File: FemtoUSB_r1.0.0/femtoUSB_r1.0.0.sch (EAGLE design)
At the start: 24 parts, among them IC1 ATSAMD21E18A-MUT

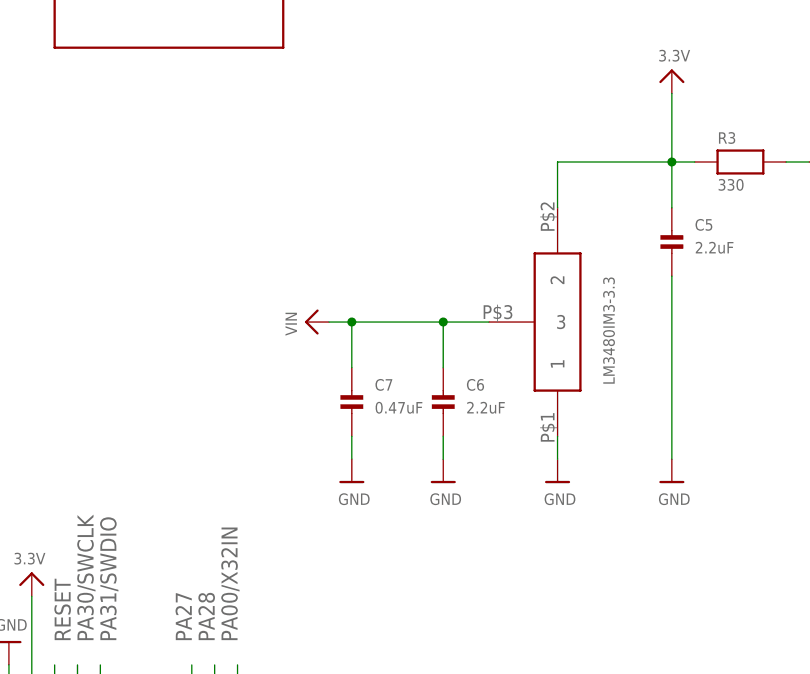
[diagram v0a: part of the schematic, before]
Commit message: Corrected the Make and model of the LDO Voltage Regulator. Board now powers on.
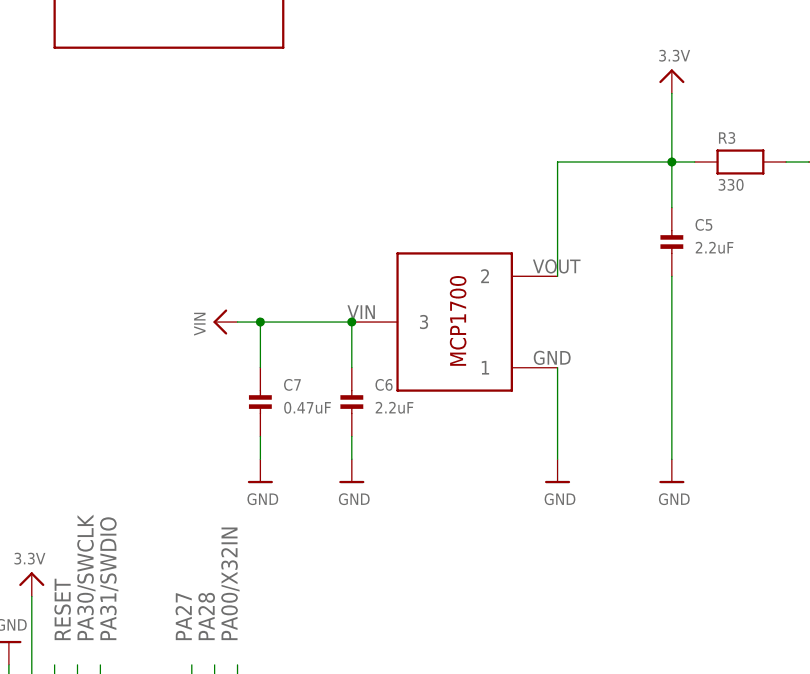
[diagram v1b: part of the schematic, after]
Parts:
- LDO_VREG: value LM3480 -> MCP1700T-3302E/TT; device ti-lm3480:LM3480 -> MCP1700T-3302E_TT:MCP1700T-3302E/TT
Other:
- moved on the sheet: C6, C7
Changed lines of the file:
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@@
 <part name="U$26" library="microbuilder" deviceset="GND" device=""/>
 <part name="U$27" library="microbuilder" deviceset="GND" device=""/>
-<part name="LDO_VREG" library="ti-lm3480" deviceset="LM3480" device=""/>
+<part name="LDO_VREG" library="MCP1700T-3302E_TT" deviceset="MCP1700T-3302E/TT" device=""/>
 <part name="U$3" library="microbuilder" deviceset="GND" device=""/>
 <part name="C5" library="microbuilder" deviceset="CAP_CERAMIC" device="_0402MP" value="2.2uF"/>
@@
 <instance part="U$26" gate="G$1" x="180.34" y="121.92" rot="R180"/>
 <instance part="U$27" gate="G$1" x="226.06" y="99.06"/>
-<instance part="LDO_VREG" gate="G$1" x="106.68" y="96.52" rot="R270"/>
+<instance part="LDO_VREG" gate="G$1" x="104.14" y="96.52" rot="R180"/>
 <instance part="U$3" gate="G$1" x="149.86" y="106.68" rot="R90"/>
 <instance part="C5" gate="G$1" x="121.92" y="96.52"/>
 <instance part="U$4" gate="G$1" x="121.92" y="116.84"/>
 <instance part="U$28" gate="G$1" x="109.22" y="71.12"/>
-<instance part="U$29" gate="G$1" x="81.28" y="88.9" rot="R90"/>
+<instance part="U$29" gate="G$1" x="71.12" y="88.9" rot="R90"/>
 <instance part="U$30" gate="G$1" x="121.92" y="71.12"/>
-<instance part="C6" gate="G$1" x="96.52" y="78.74"/>
-<instance part="C7" gate="G$1" x="86.36" y="78.74"/>
-<instance part="U$31" gate="G$1" x="96.52" y="71.12"/>
-<instance part="U$32" gate="G$1" x="86.36" y="71.12"/>
+<instance part="C6" gate="G$1" x="86.36" y="78.74"/>
+<instance part="C7" gate="G$1" x="76.2" y="78.74"/>
+<instance part="U$31" gate="G$1" x="86.36" y="71.12"/>
+<instance part="U$32" gate="G$1" x="76.2" y="71.12"/>
 <instance part="U$33" gate="G$1" x="198.12" y="43.18"/>
 <instance part="U$34" gate="G$1" x="172.72" y="165.1" rot="R90"/>
@@
 <pinref part="LDO_VREG" gate="G$1" pin="1"/>
 <pinref part="U$28" gate="G$1" pin="GND"/>
-<wire x1="109.22" y1="73.66" x2="109.22" y2="76.2" width="0.1524" layer="91"/>
+<wire x1="109.22" y1="73.66" x2="109.22" y2="83.82" width="0.1524" layer="91"/>
 </segment>
 <segment>
@@
 <pinref part="C6" gate="G$1" pin="P$2"/>
 <pinref part="U$31" gate="G$1" pin="GND"/>
-<wire x1="96.52" y1="76.2" x2="96.52" y2="73.66" width="0.1524" layer="91"/>
+<wire x1="86.36" y1="76.2" x2="86.36" y2="73.66" width="0.1524" layer="91"/>
 </segment>
 <segment>
 <pinref part="C7" gate="G$1" pin="P$2"/>
 <pinref part="U$32" gate="G$1" pin="GND"/>
-<wire x1="86.36" y1="76.2" x2="86.36" y2="73.66" width="0.1524" layer="91"/>
+<wire x1="76.2" y1="76.2" x2="76.2" y2="73.66" width="0.1524" layer="91"/>
 </segment>
 <segment>
@@
 <pinref part="U$4" gate="G$1" pin="3.3V"/>
 <pinref part="LDO_VREG" gate="G$1" pin="2"/>
-<wire x1="109.22" y1="101.6" x2="109.22" y2="106.68" width="0.1524" layer="91"/>
+<wire x1="109.22" y1="93.98" x2="109.22" y2="106.68" width="0.1524" layer="91"/>
 <wire x1="109.22" y1="106.68" x2="121.92" y2="106.68" width="0.1524" layer="91"/>
 </segment>
@@
 <segment>
 <pinref part="LDO_VREG" gate="G$1" pin="3"/>
-<wire x1="101.6" y1="88.9" x2="96.52" y2="88.9" width="0.1524" layer="91"/>
-<junction x="96.52" y="88.9"/>
-<wire x1="96.52" y1="88.9" x2="86.36" y2="88.9" width="0.1524" layer="91"/>
 <junction x="86.36" y="88.9"/>
-<wire x1="86.36" y1="88.9" x2="83.82" y2="88.9" width="0.1524" layer="91"/>
+<wire x1="86.36" y1="88.9" x2="76.2" y2="88.9" width="0.1524" layer="91"/>
+<junction x="76.2" y="88.9"/>
+<wire x1="76.2" y1="88.9" x2="73.66" y2="88.9" width="0.1524" layer="91"/>
 <pinref part="U$29" gate="G$1" pin="VIN"/>
+<wire x1="76.2" y1="88.9" x2="76.2" y2="83.82" width="0.1524" layer="91"/>
 <wire x1="86.36" y1="88.9" x2="86.36" y2="83.82" width="0.1524" layer="91"/>
-<wire x1="96.52" y1="88.9" x2="96.52" y2="83.82" width="0.1524" layer="91"/>
 <pinref part="C6" gate="G$1" pin="P$1"/>
 <pinref part="C7" gate="G$1" pin="P$1"/>

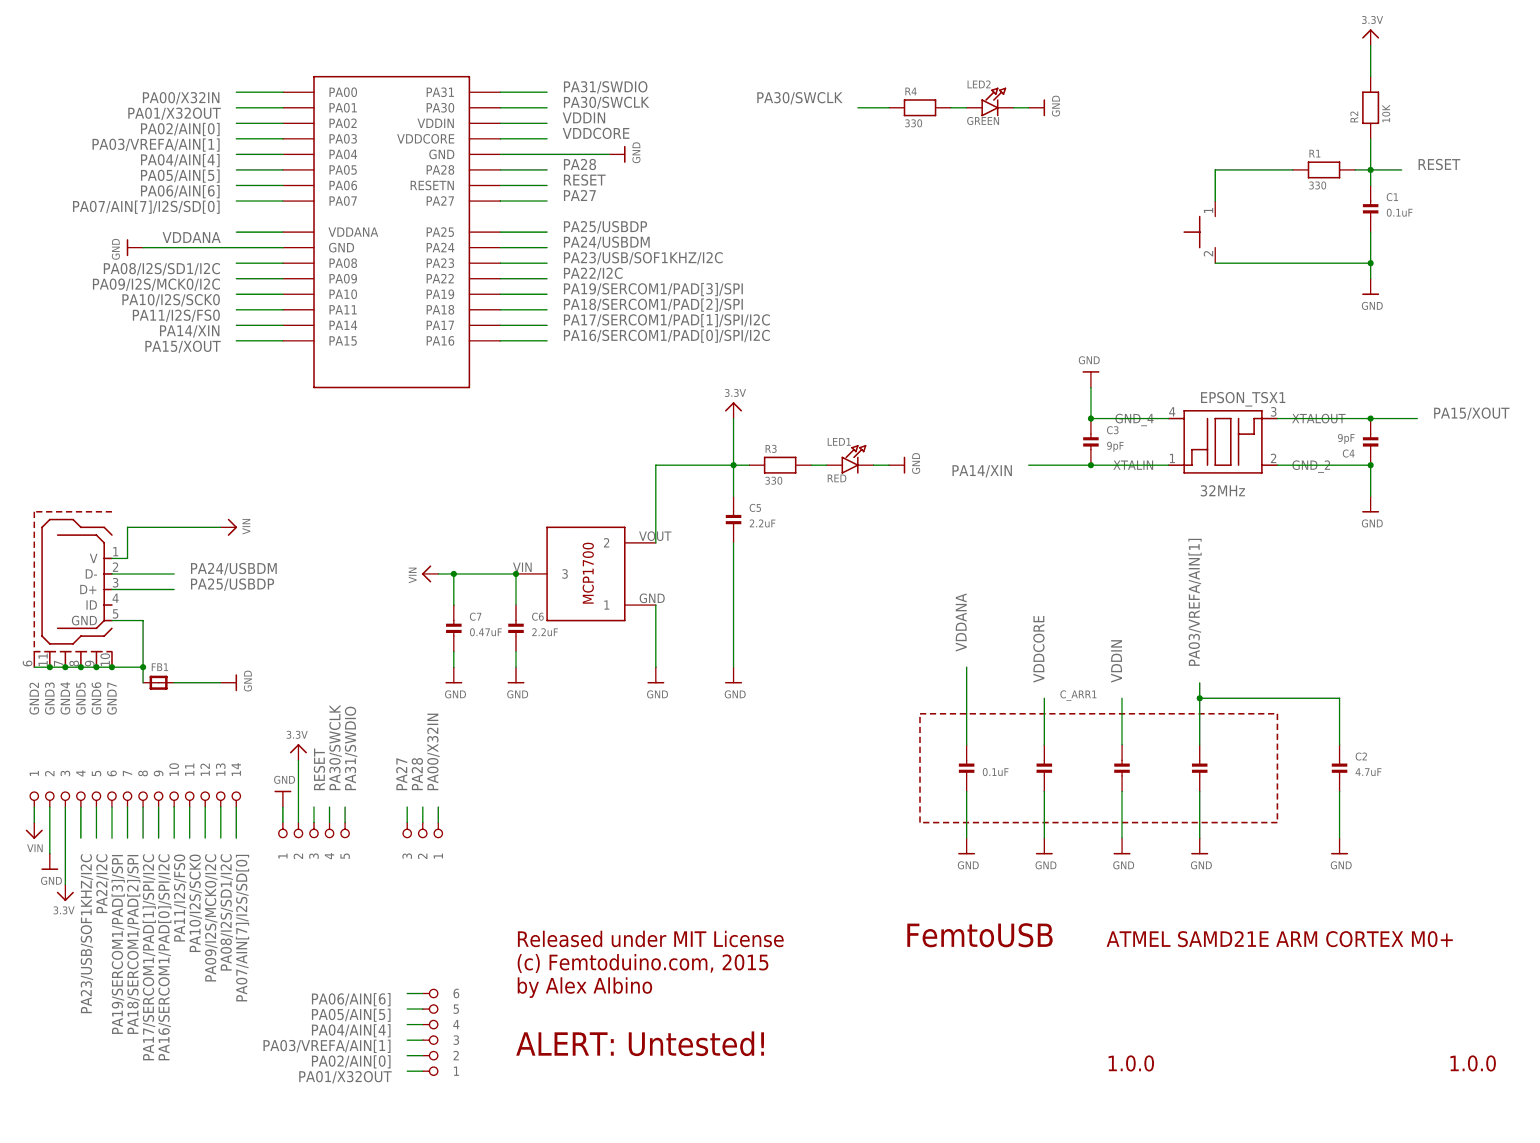
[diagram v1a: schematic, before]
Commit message: Updating the QFN (no leads) chip version of the board - adding in missing 10uF caps and 10uH inductor
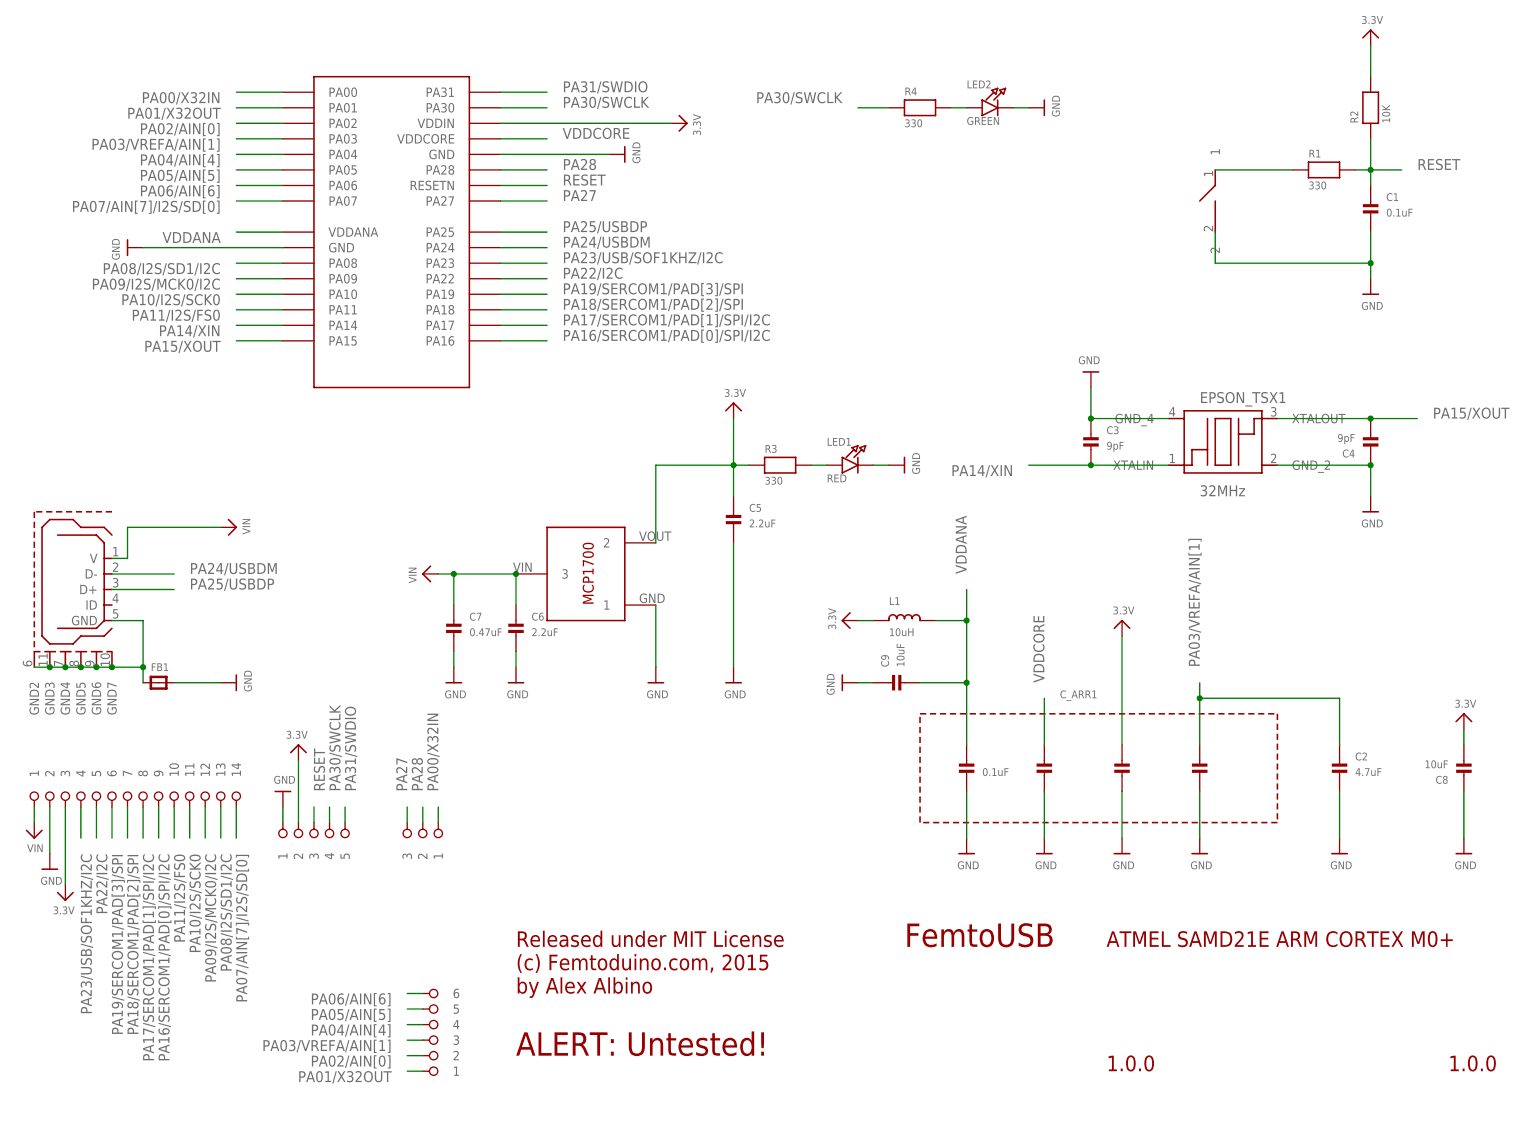
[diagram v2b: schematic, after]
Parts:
- added C8, C9: 10uF, microbuilder:CAP_CERAMIC_0402MP
- added L1: 10uH, microbuilder:INDUCTOR_0603MP
- BTN: device omron_tactile_switch:TACTILE_SWITCH_NO_GND_NO_BOSS -> femtoduino:SPST_SMD
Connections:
- removed net VDDIN: C_ARR1.P$5, IC1.VDDIN
- net 3.3V: now also C8.P$2, C_ARR1.P$5, IC1.VDDIN, L1.1
- net GND: now also C8.P$1, C9.P$1
- net VDDANA: now also C9.P$2, L1.2
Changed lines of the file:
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@@
 <part name="U$19" library="microbuilder" deviceset="3.3V" device=""/>
 <part name="C_ARR1" library="array-capacitor" deviceset="KEMET_CERAMIC_CAPACITOR_ARRAY_1X4" device="" value="0.1uF"/>
-<part name="BTN" library="omron_tactile_switch" deviceset="TACTILE_SWITCH_NO_GND_NO_BOSS" device="" value="OMRON B3U-300P(M)"/>
+<part name="BTN" library="femtoduino" deviceset="SPST_SMD" device="" value="OMRON B3U-300P(M)"/>
 <part name="U$17" library="microbuilder" deviceset="GND" device=""/>
 <part name="U$21" library="microbuilder" deviceset="GND" device=""/>
@@
 <part name="U$33" library="microbuilder" deviceset="GND" device=""/>
 <part name="U$34" library="microbuilder" deviceset="GND" device=""/>
+<part name="U$1" library="microbuilder" deviceset="3.3V" device=""/>
+<part name="U$2" library="microbuilder" deviceset="3.3V" device=""/>
+<part name="U$5" library="microbuilder" deviceset="3.3V" device=""/>
+<part name="U$20" library="microbuilder" deviceset="GND" device=""/>
+<part name="L1" library="microbuilder" deviceset="INDUCTOR" device="_0603MP" value="10uH"/>
+<part name="C9" library="microbuilder" deviceset="CAP_CERAMIC" device="_0402MP" value="10uF"/>
+<part name="U$36" library="microbuilder" deviceset="3.3V" device=""/>
+<part name="U$37" library="microbuilder" deviceset="GND" device=""/>
+<part name="C8" library="microbuilder" deviceset="CAP_CERAMIC" device="_0402MP" value="10uF"/>
 </parts>
 <sheets>
@@
 <instance part="U$33" gate="G$1" x="198.12" y="43.18"/>
 <instance part="U$34" gate="G$1" x="172.72" y="165.1" rot="R90"/>
+<instance part="U$1" gate="G$1" x="114.3" y="162.56" rot="R270"/>
+<instance part="U$2" gate="G$1" x="185.42" y="81.28"/>
+<instance part="U$5" gate="G$1" x="139.7" y="81.28" rot="R90"/>
+<instance part="U$20" gate="G$1" x="139.7" y="71.12" rot="R270"/>
+<instance part="L1" gate="G$1" x="149.86" y="81.28"/>
+<instance part="C9" gate="G$1" x="149.86" y="71.12" rot="R90"/>
+<instance part="U$36" gate="G$1" x="241.3" y="66.04"/>
+<instance part="U$37" gate="G$1" x="241.3" y="43.18"/>
+<instance part="C8" gate="G$1" x="241.3" y="58.42" rot="R180"/>
 </instances>
 <busses>
@@
 <segment>
 <pinref part="C_ARR1" gate="G$1" pin="P$1"/>
-<wire x1="160.02" y1="60.96" x2="160.02" y2="73.66" width="0.1524" layer="91"/>
-<label x="160.02" y="76.2" size="1.778" layer="95" rot="R90"/>
+<wire x1="160.02" y1="60.96" x2="160.02" y2="71.12" width="0.1524" layer="91"/>
+<label x="160.02" y="88.9" size="1.778" layer="95" rot="R90"/>
+<wire x1="160.02" y1="71.12" x2="160.02" y2="81.28" width="0.1524" layer="91"/>
+<wire x1="160.02" y1="81.28" x2="160.02" y2="86.36" width="0.1524" layer="91"/>
+<wire x1="160.02" y1="81.28" x2="154.94" y2="81.28" width="0.1524" layer="91"/>
+<wire x1="152.4" y1="71.12" x2="160.02" y2="71.12" width="0.1524" layer="91"/>
+<pinref part="L1" gate="G$1" pin="2"/>
+<pinref part="C9" gate="G$1" pin="P$2"/>
+<junction x="160.02" y="81.28"/>
+<junction x="160.02" y="71.12"/>
 </segment>
 </net>
@@
 </segment>
 </net>
-<net name="VDDIN" class="0">
-<segment>
-<pinref part="IC1" gate="G$1" pin="VDDIN"/>
-<wire x1="83.82" y1="162.56" x2="91.44" y2="162.56" width="0.1524" layer="91"/>
-<label x="93.98" y="162.56" size="1.778" layer="95"/>
-</segment>
-<segment>
-<pinref part="C_ARR1" gate="G$1" pin="P$5"/>
-<wire x1="185.42" y1="60.96" x2="185.42" y2="68.58" width="0.1524" layer="91"/>
-<label x="185.42" y="71.12" size="1.778" layer="95" rot="R90"/>
-</segment>
-</net>
 <net name="PA30/SWCLK" class="0">
 <segment>
@@
 </segment>
 <segment>
+<wire x1="200.66" y1="144.78" x2="200.66" y2="139.7" width="0.1524" layer="91"/>
 <wire x1="200.66" y1="139.7" x2="226.06" y2="139.7" width="0.1524" layer="91"/>
 <junction x="226.06" y="139.7"/>
@@
 <pinref part="U$34" gate="G$1" pin="GND"/>
 <wire x1="167.64" y1="165.1" x2="170.18" y2="165.1" width="0.1524" layer="91"/>
+</segment>
+<segment>
+<pinref part="U$20" gate="G$1" pin="GND"/>
+<wire x1="144.78" y1="71.12" x2="142.24" y2="71.12" width="0.1524" layer="91"/>
+<pinref part="C9" gate="G$1" pin="P$1"/>
+</segment>
+<segment>
+<pinref part="U$37" gate="G$1" pin="GND"/>
+<wire x1="241.3" y1="45.72" x2="241.3" y2="53.34" width="0.1524" layer="91"/>
+<pinref part="C8" gate="G$1" pin="P$1"/>
 </segment>
 </net>
@@
 <wire x1="109.22" y1="93.98" x2="109.22" y2="106.68" width="0.1524" layer="91"/>
 <wire x1="109.22" y1="106.68" x2="121.92" y2="106.68" width="0.1524" layer="91"/>
+</segment>
+<segment>
+<pinref part="IC1" gate="G$1" pin="VDDIN"/>
+<wire x1="83.82" y1="162.56" x2="111.76" y2="162.56" width="0.1524" layer="91"/>
+<pinref part="U$1" gate="G$1" pin="3.3V"/>
+</segment>
+<segment>
+<pinref part="C_ARR1" gate="G$1" pin="P$5"/>
+<wire x1="185.42" y1="60.96" x2="185.42" y2="78.74" width="0.1524" layer="91"/>
+<pinref part="U$2" gate="G$1" pin="3.3V"/>
+</segment>
+<segment>
+<pinref part="U$5" gate="G$1" pin="3.3V"/>
+<wire x1="144.78" y1="81.28" x2="142.24" y2="81.28" width="0.1524" layer="91"/>
+<pinref part="L1" gate="G$1" pin="1"/>
+</segment>
+<segment>
+<pinref part="U$36" gate="G$1" pin="3.3V"/>
+<wire x1="241.3" y1="60.96" x2="241.3" y2="63.5" width="0.1524" layer="91"/>
+<pinref part="C8" gate="G$1" pin="P$2"/>
 </segment>
 </net>
@@
 <net name="N$26" class="0">
 <segment>
-<wire x1="200.66" y1="149.86" x2="200.66" y2="154.94" width="0.1524" layer="91"/>
 <wire x1="200.66" y1="154.94" x2="213.36" y2="154.94" width="0.1524" layer="91"/>
 <pinref part="R1" gate="G$1" pin="1"/>

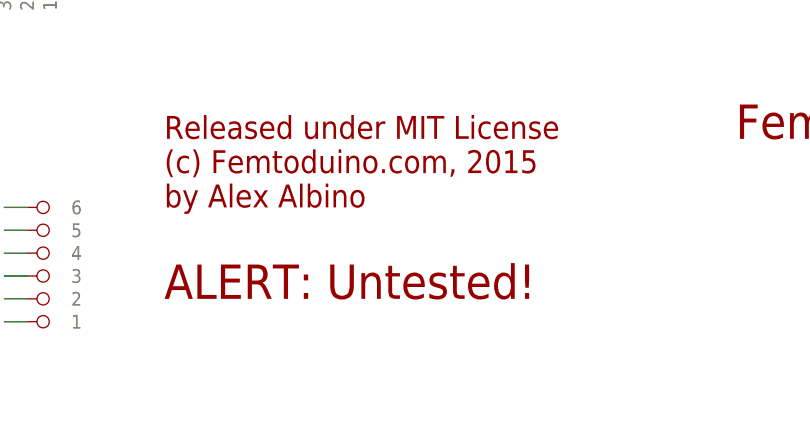
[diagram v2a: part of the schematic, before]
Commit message: Adding in PDFs, removing Notice labels, as boards appear to work now
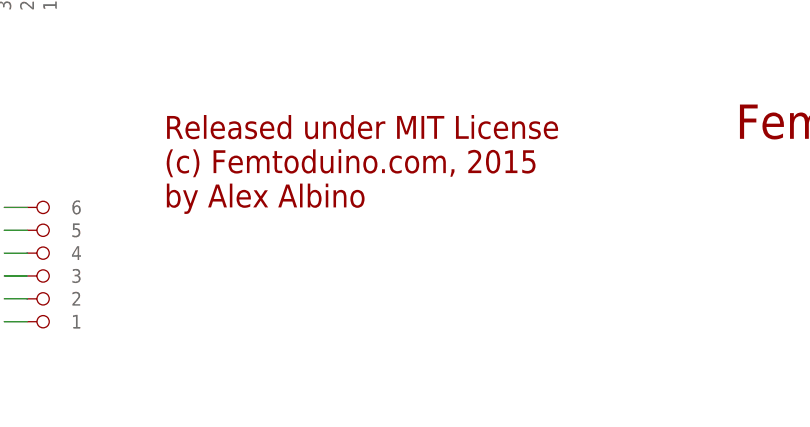
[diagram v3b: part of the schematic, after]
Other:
- note removed: "ALERT: Untested!"
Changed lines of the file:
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@@
 (c) Femtoduino.com, 2015
 by Alex Albino</text>
-<text x="86.36" y="10.16" size="3.81" layer="94" font="vector">ALERT: Untested!</text>
 </plain>
 <instances>
